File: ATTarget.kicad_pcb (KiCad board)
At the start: 2 copper layers, 28.2 x 50.8 mm, 20 parts, among them J1 ICSP, J2 Status, J3 FTDI, SW1 Power, U1 ATtiny85-20PU, U2 ATmega328-PU, Y1 16MHz

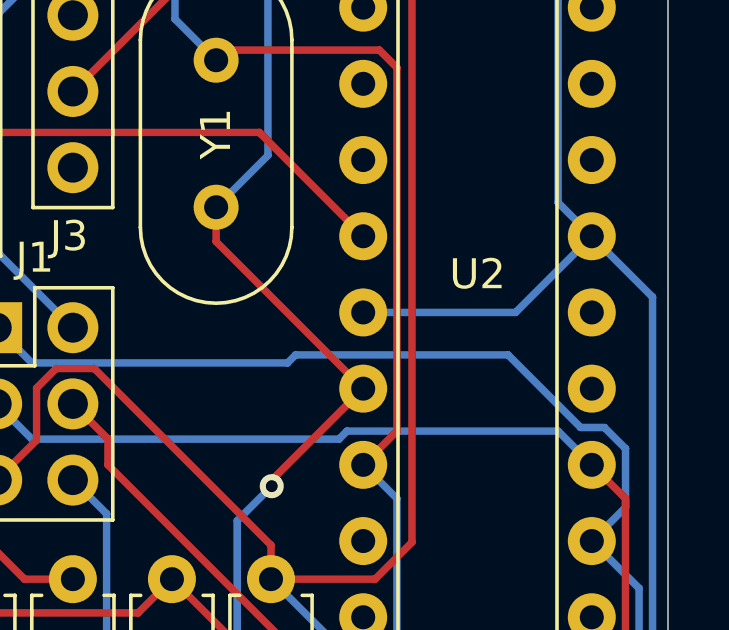
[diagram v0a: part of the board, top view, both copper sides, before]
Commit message: Connect AVCC to V+.
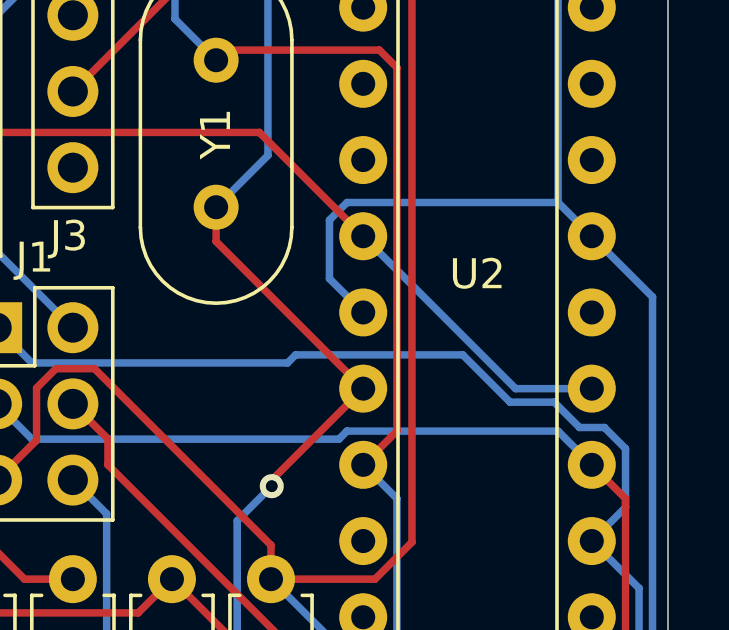
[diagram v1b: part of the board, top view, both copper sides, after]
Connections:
- U2 pad 20: Net-(U2-Pad20) -> /V+
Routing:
- net /V+: track 77.5 -> 87.2 mm
- net GND: track 128.2 -> 130.9 mm
